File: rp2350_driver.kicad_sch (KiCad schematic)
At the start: 291 parts, among them J1 XT30, J10 Power Output, J11 CAN2 PLUG, J12 Conn_01x06, J2 XT30, J3 USB_C_Receptacle_USB2.0, J4 SM03B-SRSS-TB, J5 Estop Conn, J6 SM03B-SRSS-TB, J7 Conn_01x03, J8 Conn_01x03, J9 XT30, Q1 Q_PNP_BEC, Q2 Q_PNP_BEC, Q3 Q_PNP_BEC, Q4 Q_PNP_BEC, Q5 Q_NMOS_GDS, SW1 Button, SW2 Button, U1 EG3113, U10 INA240A1D, U101 FUSB302BMPX, U11 USBLC6-2P6, U12 EG3113, U13 TS5A3159DCK, U14 TS5A3159DCK, U15 TS5A3159DCK, U16 CA-IS3052CG, U17 TS5A3159DCK, U18 SIT3088ETK, U19 SIT3088ETK, U20 SIT3088ETK, U21 SIT3088ETK, U22 TS5A3159DCK, U23 TS5A3159DCK, U24 TS5A3159DCK, U25 TS5A3159DCK, U26 TS5A3159DCK, U27 TS5A3159DCK, U28 XL7005A, U29 LM74700, U3 W25Q16JV, U4 SPX3819M5-L-3-3, U5 INA240A1D, U6 EG3113, U7 EG3113, U8 RP2350_80QFN, U9 INA240A1D, Y1 ABM8-272-T3

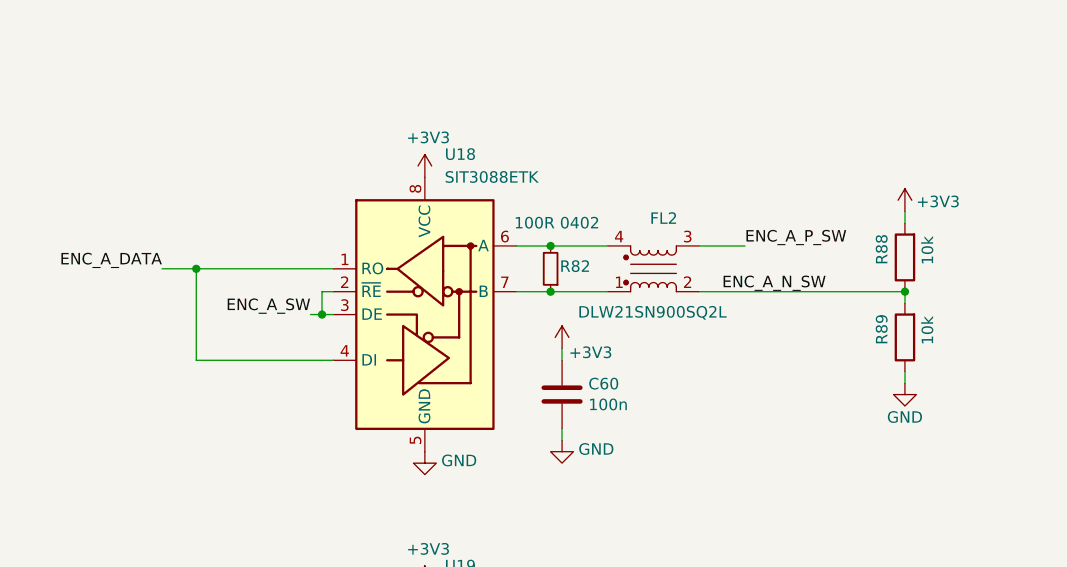
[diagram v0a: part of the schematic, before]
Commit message: Whether inadvisedly or not, I have ordered this rev
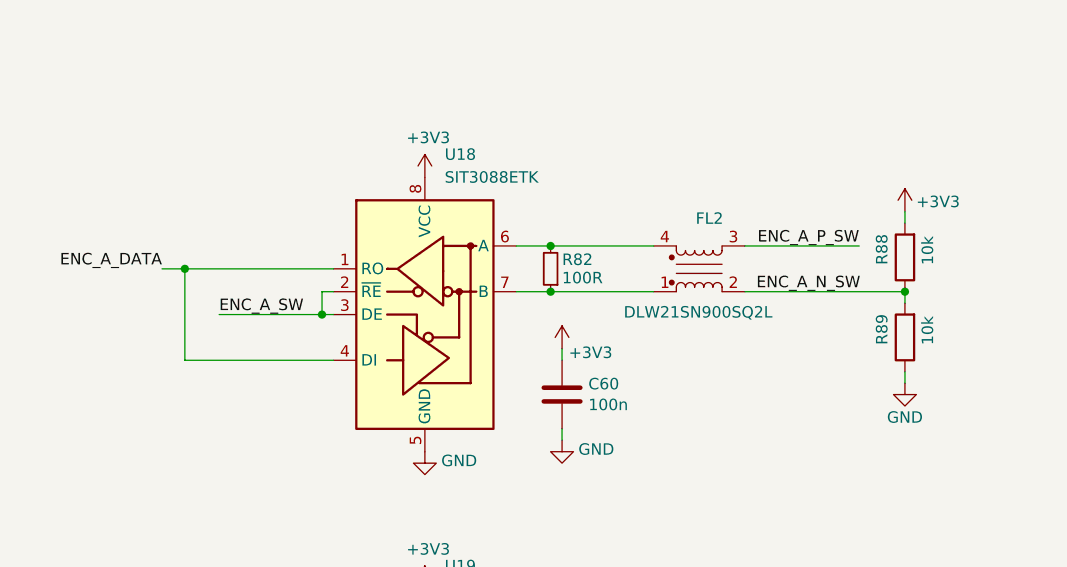
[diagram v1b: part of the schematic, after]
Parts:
- R82: value 100R 0402 -> 100R
- U18: footprint parts:DFN-8_L3.0-W3.0-P0.65-BL-EP -> Package_SO:MSOP-8-1EP_3x3mm_P0.65mm_EP1.5x1.8mm
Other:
- moved on the sheet: FL2
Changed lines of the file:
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@@
 	)
 	(junction
-		(at 579.12 267.97)
-		(diameter 0)
-		(color 0 0 0 0)
-	)
-	(junction
 		(at 190.5 509.27)
 		(diameter 0)
@@
 	)
 	(junction
+		(at 577.85 267.97)
+		(diameter 0)
+		(color 0 0 0 0)
+	)
+	(junction
 		(at 234.95 478.79)
 		(diameter 0)
@@
 	(wire
 		(pts
-			(xy 618.49 265.43) (xy 624.84 265.43)
+			(xy 618.49 265.43) (xy 629.92 265.43)
 		)
 		(stroke
@@
 	(wire
 		(pts
-			(xy 635 265.43) (xy 640.08 265.43)
+			(xy 640.08 265.43) (xy 652.78 265.43)
 		)
 		(stroke
@@
 	(wire
 		(pts
-			(xy 579.12 278.13) (xy 594.36 278.13)
+			(xy 577.85 278.13) (xy 594.36 278.13)
 		)
 		(stroke
@@
 	(wire
 		(pts
-			(xy 635 270.51) (xy 657.86 270.51)
+			(xy 640.08 270.51) (xy 657.86 270.51)
 		)
 		(stroke
@@
 	(wire
 		(pts
+			(xy 577.85 267.97) (xy 594.36 267.97)
+		)
+		(stroke
+			(width 0)
+			(type default)
+		)
+	)
+	(wire
+		(pts
 			(xy 321.31 138.43) (xy 332.74 138.43)
 		)
@@
 	(wire
 		(pts
-			(xy 579.12 267.97) (xy 594.36 267.97)
-		)
-		(stroke
-			(width 0)
-			(type default)
-		)
-	)
-	(wire
-		(pts
 			(xy 393.7 267.97) (xy 389.89 267.97)
 		)
@@
 	(wire
 		(pts
-			(xy 618.49 270.51) (xy 624.84 270.51)
+			(xy 618.49 270.51) (xy 629.92 270.51)
 		)
 		(stroke
@@
 	(wire
 		(pts
-			(xy 579.12 267.97) (xy 579.12 278.13)
+			(xy 577.85 267.97) (xy 577.85 278.13)
 		)
 		(stroke
@@
 	(wire
 		(pts
-			(xy 575.31 267.97) (xy 579.12 267.97)
+			(xy 575.31 267.97) (xy 577.85 267.97)
 		)
 		(stroke
@@
 	(wire
 		(pts
-			(xy 591.82 273.05) (xy 593.09 273.05)
+			(xy 581.66 273.05) (xy 593.09 273.05)
 		)
 		(stroke
@@
 	)
 	(label "ENC_A_P_SW"
-		(at 640.08 265.43 0)
+		(at 652.78 265.43 180)
 		(effects
 			(font
 				(size 1.27 1.27)
 			)
-			(justify left bottom)
+			(justify right bottom)
 		)
 	)
@@
 	)
 	(label "ENC_A_N_SW"
-		(at 637.54 270.51 0)
+		(at 641.35 270.51 0)
 		(effects
 			(font
@@
 	)
 	(label "ENC_A_SW"
-		(at 591.82 273.05 180)
+		(at 581.66 273.05 0)
 		(effects
 			(font
 				(size 1.27 1.27)
 			)
-			(justify right bottom)
+			(justify left bottom)
 		)
 	)
@@
 			)
 		)
-		(property "Footprint" "parts:DFN-8_L3.0-W3.0-P0.65-BL-EP"
+		(property "Footprint" "Package_SO:MSOP-8-1EP_3x3mm_P0.65mm_EP1.5x1.8mm"
 			(at 604.52 295.91 0)
 			(effects
@@
 		(dnp no)
 		(property "Reference" "R82"
-			(at 619.506 267.7159 0)
+			(at 619.76 266.9539 0)
 			(effects
 				(font
@@
 			)
 		)
-		(property "Value" "100R 0402"
-			(at 614.426 262.8899 0)
+		(property "Value" "100R"
+			(at 619.76 268.9859 0)
 			(effects
 				(font
@@
 	(symbol
 		(lib_id "Device:Filter_EMI_CommonMode")
-		(at 629.92 267.97 0)
+		(at 635 267.97 0)
 		(mirror x)
 		(unit 1)
@@
 		(dnp no)
 		(property "Reference" "FL2"
-			(at 631.063 262.382 0)
+			(at 636.143 262.382 0)
 			(effects
 				(font
@@
 		)
 		(property "Value" "DLW21SN900SQ2L"
-			(at 629.793 272.796 0)
+			(at 634.873 272.796 0)
 			(effects
 				(font
@@
 		)
 		(property "Footprint" "parts:FILTER-SMD_4P-L2.0-W1.2-BL_DLW21H"
-			(at 629.92 268.986 0)
+			(at 635 268.986 0)
 			(effects
 				(font
@@
 		)
 		(property "Datasheet" "~"
-			(at 629.92 268.986 0)
+			(at 635 268.986 0)
 			(effects
 				(font
@@
 		)
 		(property "Description" "EMI 2-inductor common mode filter"
-			(at 629.92 267.97 0)
+			(at 635 267.97 0)
 			(effects
 				(font
@@
 		)
 		(property "LCSC" "C97856"
-			(at 629.92 267.97 0)
+			(at 635 267.97 0)
 			(effects
 				(font

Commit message: Fix a few parts as per corrections made during order.
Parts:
- C4, C49, C50, C52, C59, C60, C61, C62, C63, C64, C65, C66, C71, C72, C73: LCSC C14663 -> C131394
- C42, C80: value 220uF 63V solid -> 100uF 100V; LCSC C5455531 -> C2887236
- U18: footprint Package_SO:MSOP-8-1EP_3x3mm_P0.65mm_EP1.5x1.8mm -> parts:DFN-8_L3.0-W3.0-P0.65-BL-EP
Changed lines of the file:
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@@
 			)
 		)
-		(property "Footprint" "Package_SO:MSOP-8-1EP_3x3mm_P0.65mm_EP1.5x1.8mm"
+		(property "Footprint" "parts:DFN-8_L3.0-W3.0-P0.65-BL-EP"
 			(at 604.52 295.91 0)
 			(effects
@@
 			)
 		)
-		(property "LCSC" "C14663"
+		(property "LCSC" "C131394"
 			(at 668.02 486.41 0)
 			(effects
@@
 			)
 		)
-		(property "LCSC" "C14663"
+		(property "LCSC" "C131394"
 			(at 699.77 422.91 0)
 			(effects
@@
 			)
 		)
-		(property "LCSC" "C14663"
+		(property "LCSC" "C131394"
 			(at 114.3 264.16 0)
 			(effects
@@
 			)
 		)
-		(property "LCSC" "C14663"
+		(property "LCSC" "C131394"
 			(at 618.49 421.64 0)
 			(effects
@@
 			)
 		)
-		(property "Value" "220uF 63V solid"
+		(property "Value" "100uF 100V"
 			(at 348.996 487.934 90)
 			(effects
@@
 			)
 		)
-		(property "LCSC" "C5455531"
+		(property "LCSC" "C2887236"
 			(at 354.33 481.33 0)
 			(effects
@@
 			)
 		)
-		(property "LCSC" "C14663"
+		(property "LCSC" "C131394"
 			(at 715.01 314.96 0)
 			(effects
@@
 			)
 		)
-		(property "LCSC" "C14663"
+		(property "LCSC" "C131394"
 			(at 669.29 453.39 0)
 			(effects
@@
 			)
 		)
-		(property "LCSC" "C14663"
+		(property "LCSC" "C131394"
 			(at 619.76 281.94 0)
 			(effects
@@
 			)
 		)
-		(property "LCSC" "C14663"
+		(property "LCSC" "C131394"
 			(at 496.57 180.34 0)
 			(effects
@@
 			)
 		)
-		(property "LCSC" "C14663"
+		(property "LCSC" "C131394"
 			(at 713.74 278.13 0)
 			(effects
@@
 			)
 		)
-		(property "LCSC" "C14663"
+		(property "LCSC" "C131394"
 			(at 697.23 355.6 0)
 			(effects
@@
 			)
 		)
-		(property "LCSC" "C14663"
+		(property "LCSC" "C131394"
 			(at 619.76 327.66 0)
 			(effects
@@
 			)
 		)
-		(property "LCSC" "C14663"
+		(property "LCSC" "C131394"
 			(at 712.47 241.3 0)
 			(effects
@@
 			)
 		)
-		(property "LCSC" "C14663"
+		(property "LCSC" "C131394"
 			(at 618.49 375.92 0)
 			(effects
@@
 			)
 		)
-		(property "LCSC" "C14663"
+		(property "LCSC" "C131394"
 			(at 782.32 257.81 0)
 			(effects
@@
 			)
 		)
-		(property "Value" "220uF 63V solid"
+		(property "Value" "100uF 100V"
 			(at 359.156 487.934 90)
 			(effects
@@
 			)
 		)
-		(property "LCSC" "C5455531"
+		(property "LCSC" "C2887236"
 			(at 364.49 481.33 0)
 			(effects
@@
 			)
 		)
-		(property "LCSC" "C14663"
+		(property "LCSC" "C131394"
 			(at 698.5 388.62 0)
 			(effects

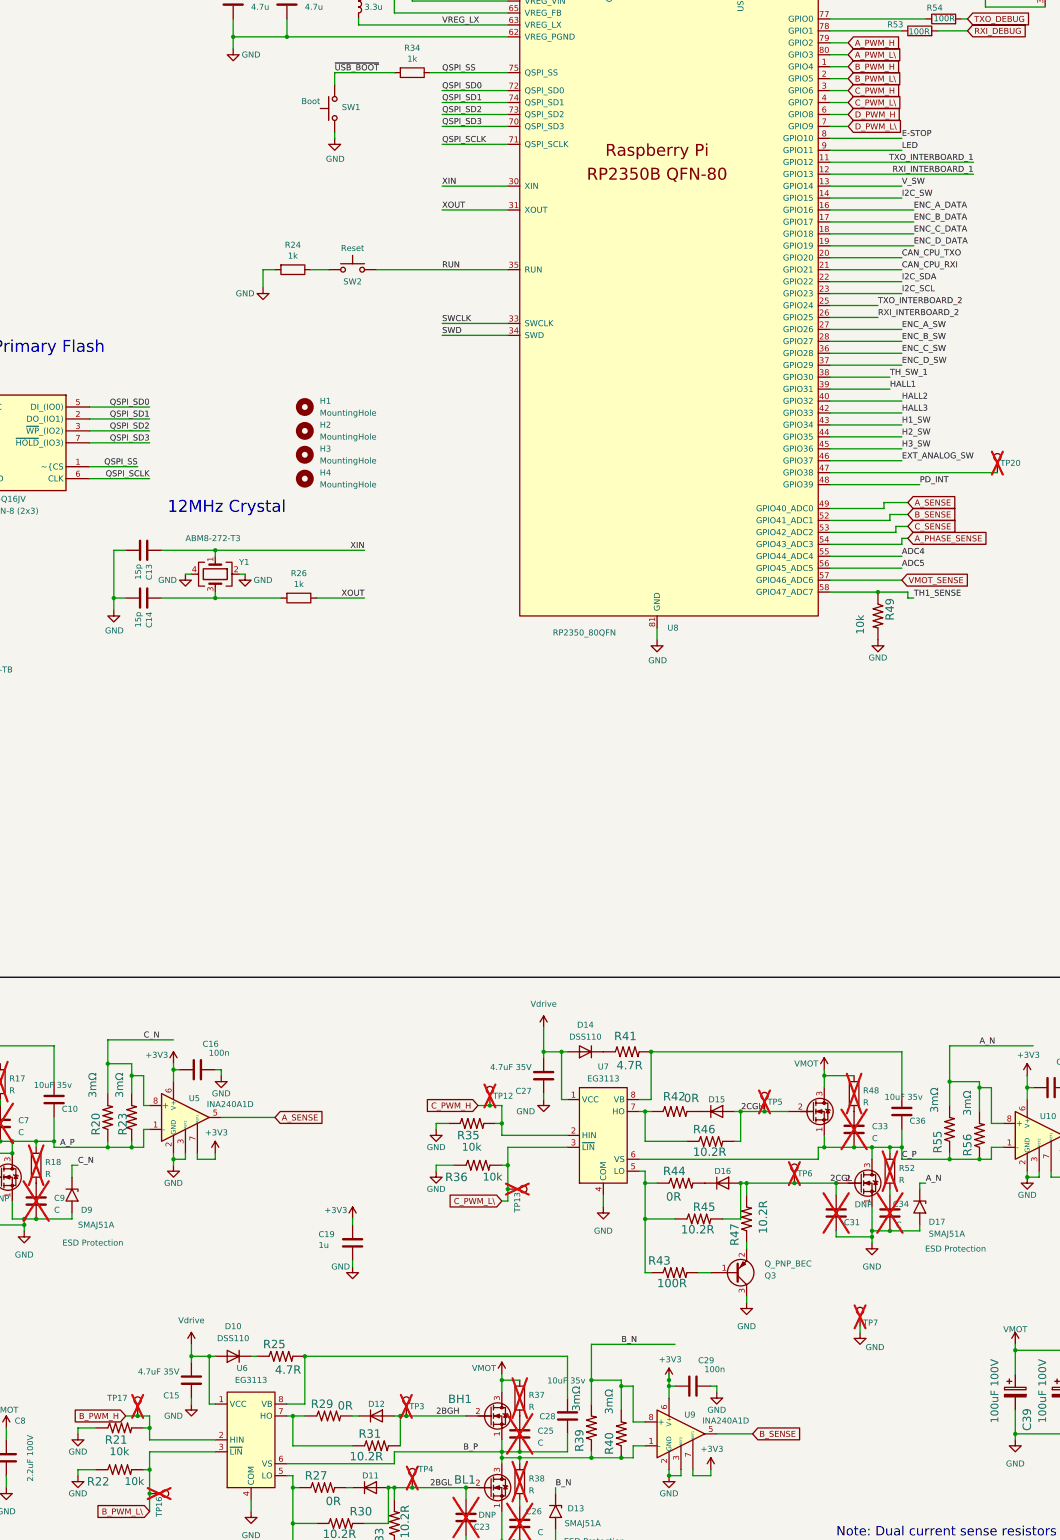
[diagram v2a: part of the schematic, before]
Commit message: Add encoder plus updated motor driver files.
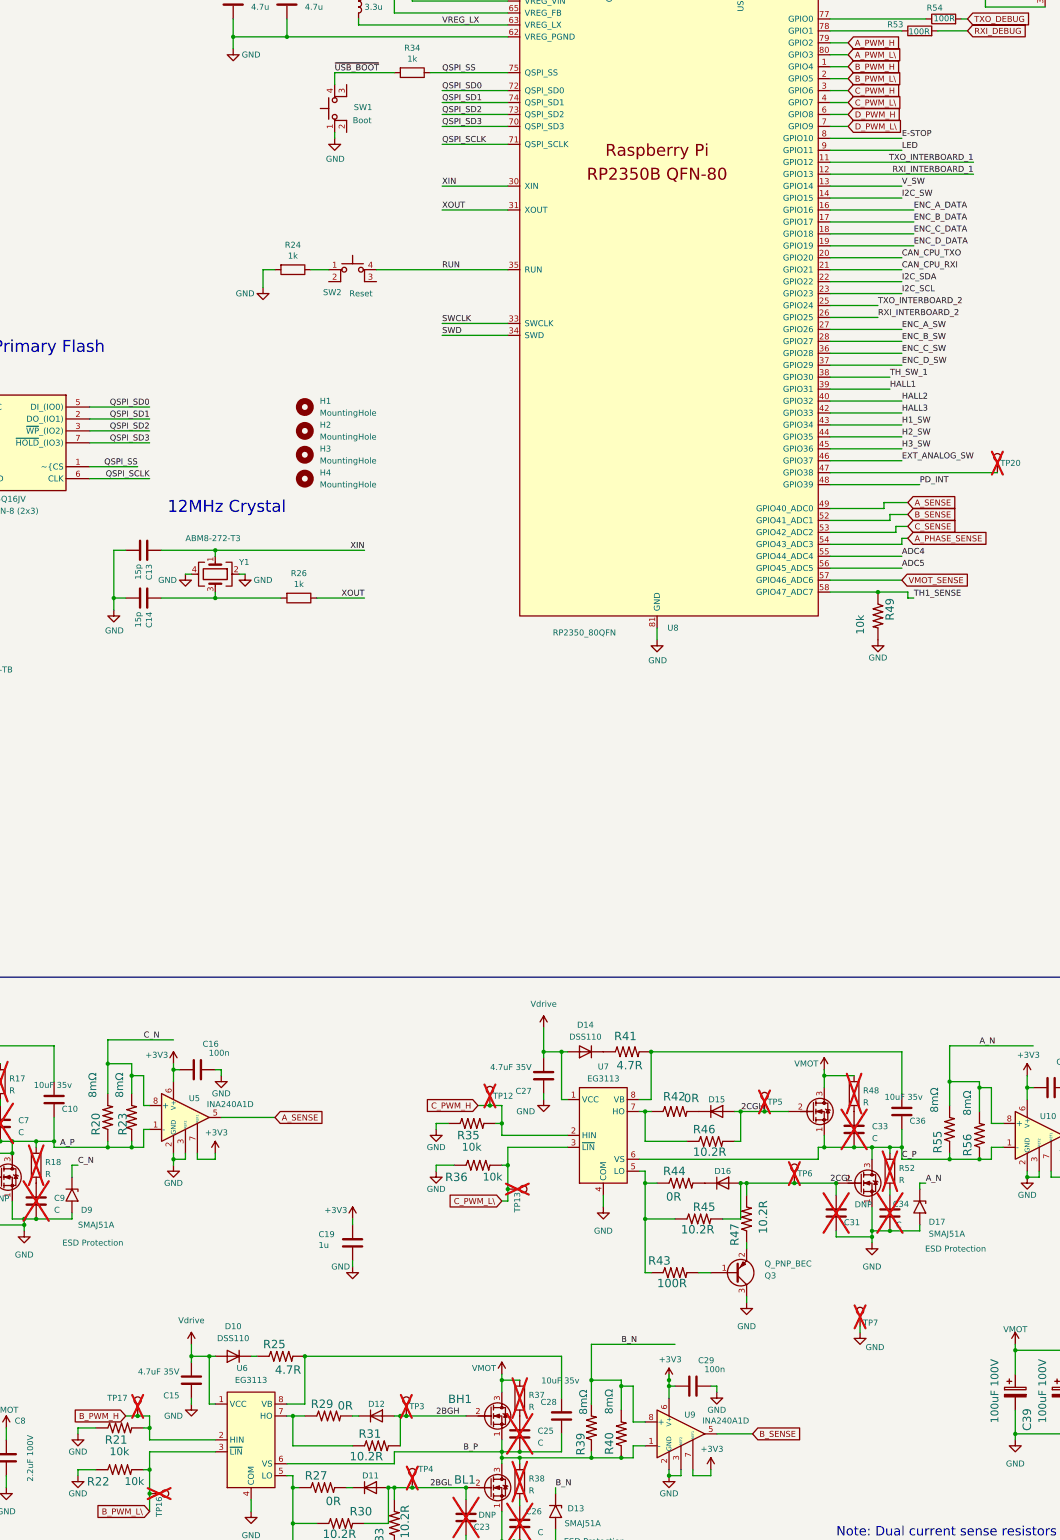
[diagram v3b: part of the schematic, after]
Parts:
- R20, R23, R39, R40, R55, R56: value 3mΩ -> 8mΩ; LCSC C2688862 -> C2904240
- SW1, SW2: symbol Switch:SW_Push -> Switch:SW_MEC_5E
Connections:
- net RUN: now also SW2.4 (A); no longer SW2.2
- net ~{USB_BOOT}: now also SW1.4 (A); no longer SW1.2
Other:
- moved on the sheet: C28
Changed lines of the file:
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@@
 	(wire
 		(pts
-			(xy 238.76 494.03) (xy 248.92 494.03)
+			(xy 238.76 494.03) (xy 247.65 494.03)
 		)
 		(stroke
@@
 	(wire
 		(pts
-			(xy 193.04 473.71) (xy 248.92 473.71)
+			(xy 193.04 473.71) (xy 247.65 473.71)
 		)
 		(stroke
@@
 	(wire
 		(pts
-			(xy 248.92 482.6) (xy 248.92 473.71)
+			(xy 247.65 482.6) (xy 247.65 473.71)
 		)
 		(stroke
@@
 	(wire
 		(pts
-			(xy 248.92 494.03) (xy 248.92 490.22)
+			(xy 247.65 494.03) (xy 247.65 490.22)
 		)
 		(stroke
@@
 			)
 		)
-		(property "Value" "3mΩ"
+		(property "Value" "8mΩ"
 			(at 332.994 422.529 0)
 			(effects
@@
 			)
 		)
-		(property "LCSC" "C2688862"
+		(property "LCSC" "C2904240"
 			(at 336.55 426.72 0)
 			(effects
@@
 			)
 		)
-		(property "Value" "3mΩ"
+		(property "Value" "8mΩ"
 			(at 152.654 418.719 0)
 			(effects
@@
 			)
 		)
-		(property "LCSC" "C2688862"
+		(property "LCSC" "C2904240"
 			(at 156.21 422.91 0)
 			(effects
@@
 	)
 	(symbol
-		(lib_id "Switch:SW_Push")
-		(at 203.2 242.57 0)
+		(lib_id "Switch:SW_MEC_5E")
+		(at 203.2 245.11 0)
 		(unit 1)
 		(exclude_from_sim no)
@@
 		(dnp no)
 		(property "Reference" "SW2"
-			(at 203.2 245.11 0)
+			(at 198.882 247.396 0)
 			(effects
 				(font
@@
 		)
 		(property "Value" "Button"
-			(at 203.2 237.744 0)
+			(at 203.2 240.284 0)
 			(effects
 				(font
@@
 			)
 		)
-		(property "Datasheet" "~"
+		(property "Datasheet" "http://www.apem.com/int/index.php?controller=attachment&id_attachment=1371"
 			(at 203.2 237.49 0)
 			(effects
@@
 			)
 		)
-		(property "Description" ""
-			(at 203.2 242.57 0)
+		(property "Description" "MEC 5E single pole normally-open tactile switch"
+			(at 203.2 245.11 0)
 			(effects
 				(font
@@
 		)
 		(property "LCSC" "C19724063"
-			(at 203.2 242.57 0)
+			(at 203.2 245.11 0)
 			(effects
 				(font
@@
 		)
 		(property "Name" "Reset"
-			(at 203.2 237.998 0)
+			(at 204.978 247.65 0)
 			(effects
 				(font
@@
 		(pin "2"
 		)
+		(pin "4"
+		)
+		(pin "3"
+		)
 		(instances
 			(project "integrated_driver"
@@
 			)
 		)
-		(property "Value" "3mΩ"
+		(property "Value" "8mΩ"
 			(at 146.939 418.719 0)
 			(effects
@@
 			)
 		)
-		(property "LCSC" "C2688862"
+		(property "LCSC" "C2904240"
 			(at 151.13 422.91 0)
 			(effects
@@
 	(symbol
 		(lib_id "Device:C")
-		(at 248.92 486.41 180)
+		(at 247.65 486.41 180)
 		(unit 1)
 		(exclude_from_sim no)
@@
 		(dnp no)
 		(property "Reference" "C28"
-			(at 246.38 485.775 0)
+			(at 246.634 482.727 0)
 			(effects
 				(font
@@
 		)
 		(property "Value" "10uF 35v"
-			(at 252.73 478.155 0)
+			(at 251.46 478.155 0)
 			(effects
 				(font
@@
 		)
 		(property "Footprint" "Capacitor_SMD:C_0603_1608Metric"
-			(at 247.9548 482.6 0)
+			(at 246.6848 482.6 0)
 			(effects
 				(font
@@
 		)
 		(property "Datasheet" "~"
-			(at 248.92 486.41 0)
+			(at 247.65 486.41 0)
 			(effects
 				(font
@@
 		)
 		(property "Description" ""
-			(at 248.92 486.41 0)
+			(at 247.65 486.41 0)
 			(effects
 				(font
@@
 		)
 		(property "LCSC" "C194427"
-			(at 248.92 486.41 0)
+			(at 247.65 486.41 0)
 			(effects
 				(font
@@
 		(dnp no)
 		(property "Reference" "R39"
-			(at 252.5014 494.03 0)
+			(at 252.7554 494.792 0)
 			(effects
 				(font
@@
 			)
 		)
-		(property "Value" "3mΩ"
-			(at 249.809 485.394 0)
+		(property "Value" "8mΩ"
+			(at 251.333 486.156 0)
 			(effects
 				(font
@@
 			)
 		)
-		(property "LCSC" "C2688862"
+		(property "LCSC" "C2904240"
 			(at 254 488.95 0)
 			(effects
@@
 	)
 	(symbol
-		(lib_id "Switch:SW_Push")
-		(at 199.39 208.28 90)
+		(lib_id "Switch:SW_MEC_5E")
+		(at 201.93 208.28 90)
 		(unit 1)
 		(exclude_from_sim no)
@@
 		(dnp no)
 		(property "Reference" "SW1"
-			(at 200.914 208.0259 90)
+			(at 203.454 208.0259 90)
 			(effects
 				(font
@@
 		)
 		(property "Value" "Button"
-			(at 192.278 206.5019 90)
+			(at 194.818 206.5019 90)
 			(effects
 				(font
@@
 			)
 		)
-		(property "Datasheet" "~"
+		(property "Datasheet" "http://www.apem.com/int/index.php?controller=attachment&id_attachment=1371"
 			(at 194.31 208.28 0)
 			(effects
@@
 			)
 		)
-		(property "Description" ""
-			(at 199.39 208.28 0)
+		(property "Description" "MEC 5E single pole normally-open tactile switch"
+			(at 201.93 208.28 0)
 			(effects
 				(font
@@
 		)
 		(property "LCSC" "C19724063"
-			(at 199.39 208.28 90)
+			(at 201.93 208.28 90)
 			(effects
 				(font
@@
 		)
 		(property "Name" "Boot"
-			(at 194.31 206.756 90)
+			(at 205.232 210.82 90)
 			(effects
 				(font
@@
 		(pin "2"
 		)
+		(pin "4"
+		)
+		(pin "3"
+		)
 		(instances
 			(project "integrated_driver"
@@
 			)
 		)
-		(property "Value" "3mΩ"
+		(property "Value" "8mΩ"
 			(at 256.794 486.029 0)
 			(effects
@@
 			)
 		)
-		(property "LCSC" "C2688862"
+		(property "LCSC" "C2904240"
 			(at 260.35 490.22 0)
 			(effects
@@
 			)
 		)
-		(property "Value" "3mΩ"
+		(property "Value" "8mΩ"
 			(at 326.009 421.894 0)
 			(effects
@@
 			)
 		)
-		(property "LCSC" "C2688862"
+		(property "LCSC" "C2904240"
 			(at 330.2 425.45 0)
 			(effects
